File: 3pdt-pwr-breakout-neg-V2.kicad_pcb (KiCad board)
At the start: 2 copper layers, 40 x 21.5 mm, 42 parts, among them Q1 DMP3099L, SW1 SW_3PDT, U1 TLV76701DRVR, U2 LM2664M6X/NOPB, U3 LM2664M6X/NOPB

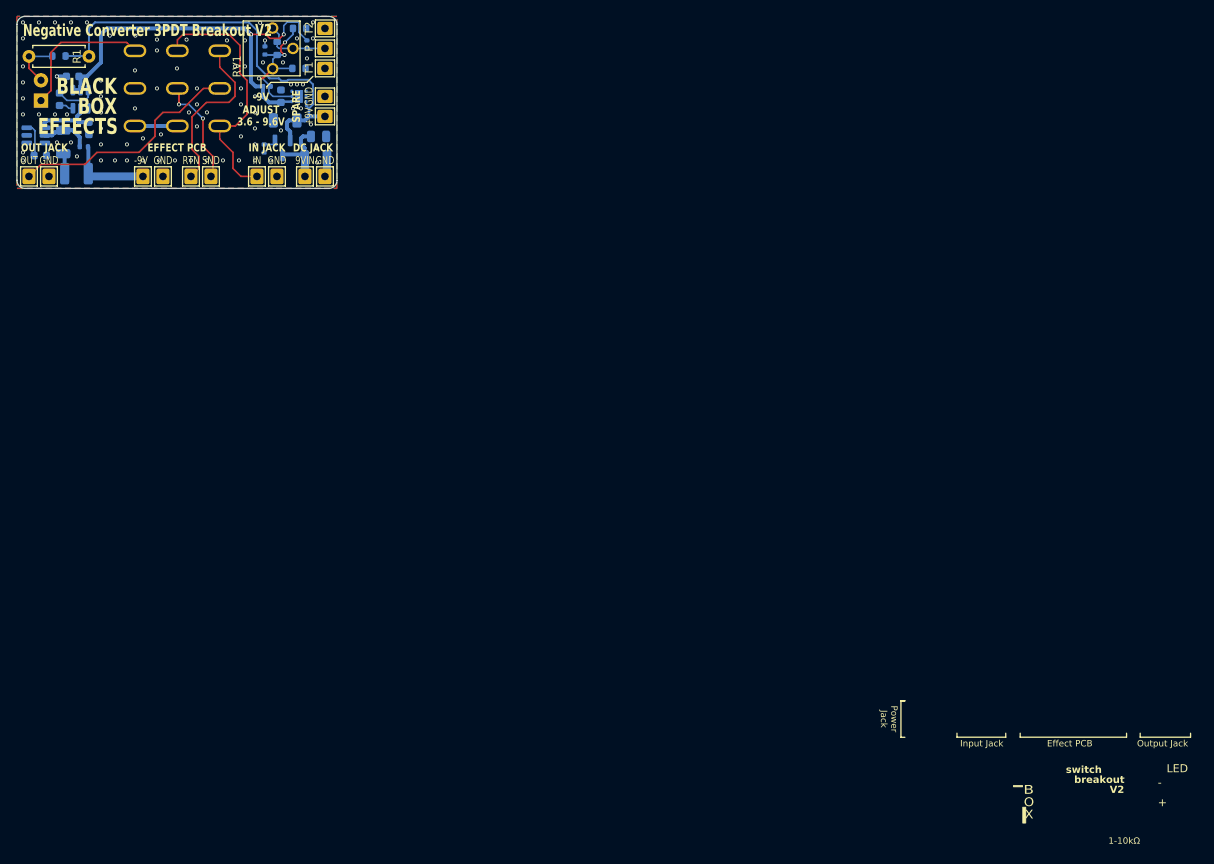
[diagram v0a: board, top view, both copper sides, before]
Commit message: Moved wire pads, clearing warnings. Good to fab?
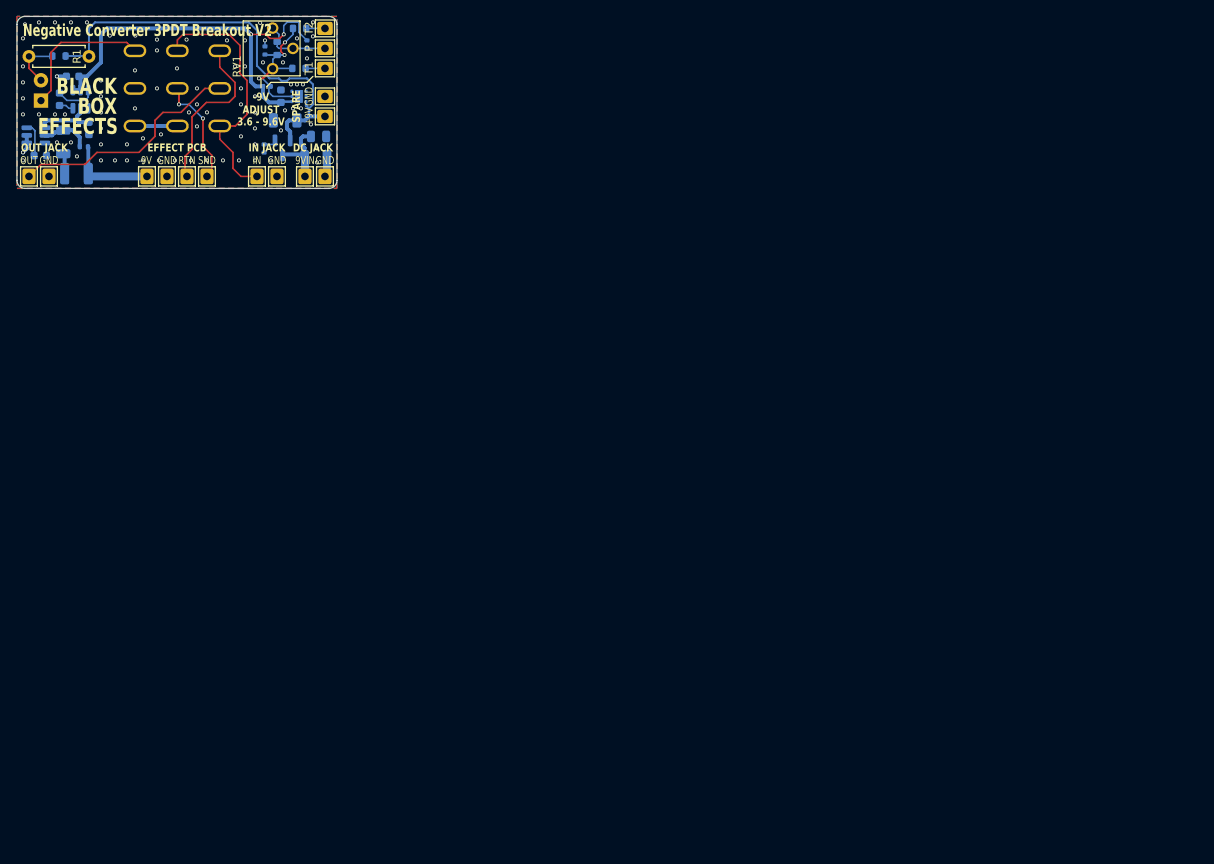
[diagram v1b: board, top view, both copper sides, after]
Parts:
- C10, C4, C5, C7: value 2.2u -> 1u
- moved WP10 0.50 mm to (66.2, 71.0)
- moved WP7 0.50 mm to (68.8, 71.0)
- moved WP8 0.50 mm to (71.2, 71.0)
- moved WP9 0.50 mm to (63.8, 71.0)
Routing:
- net Net-(R7-Pad1): track 0.00 -> 2.42 mm
- net Net-(R8-Pad1): track 0.00 -> 2.35 mm
- net GND: track 7.37 -> 9.69 mm
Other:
- board text removed: "+"
- board text removed: "-"
- board text removed: "1-10kΩ"
- board text removed: "B"
- board text removed: "Effect PCB"
- board text removed: "Input Jack"
- board text removed: "O"
- board text removed: "Output Jack"
- board text removed: "Power Jack"
- board text removed: "V2"
- board text removed: "X"
- board text removed: "breakout"
- board text removed: "switch"

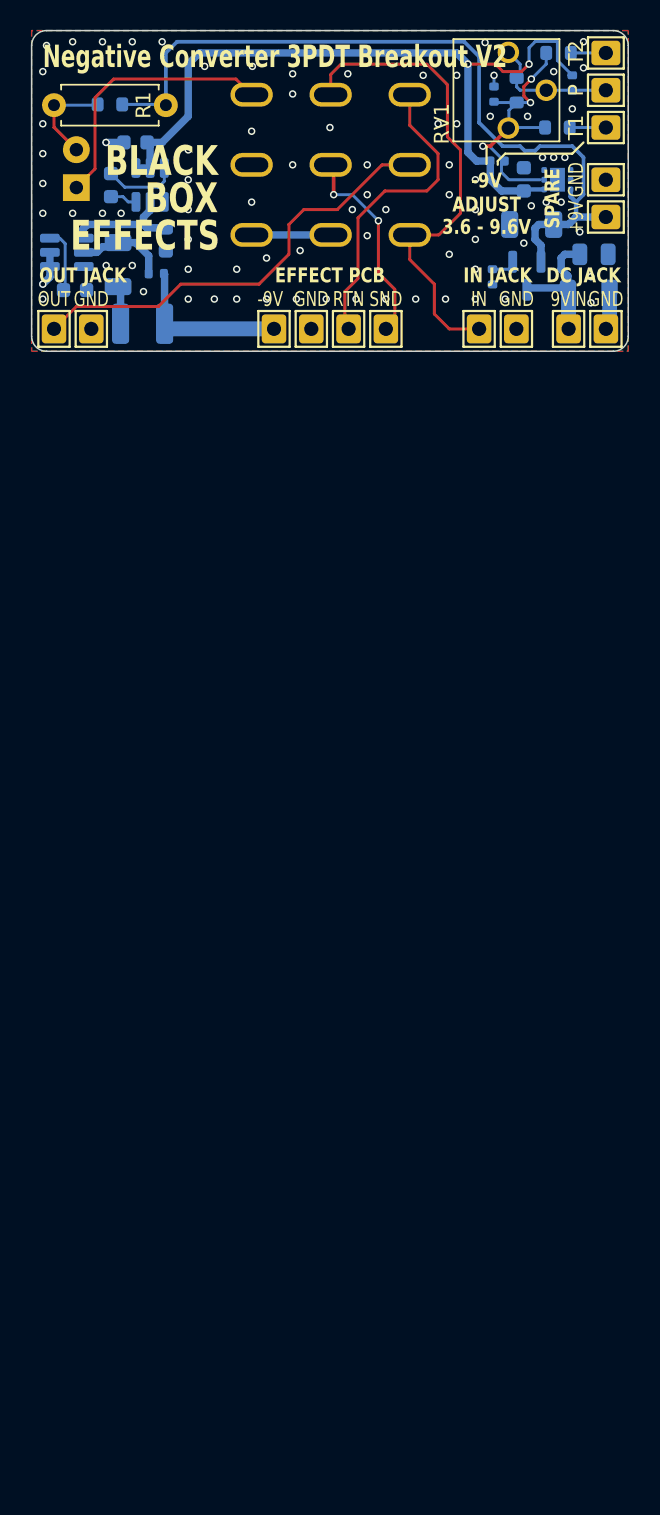
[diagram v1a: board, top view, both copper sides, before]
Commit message: Changed LDO and added negative LDO
Changed LDO to a leaded package and added an optional negative LDO. Layout changes implemented, going to review and order.
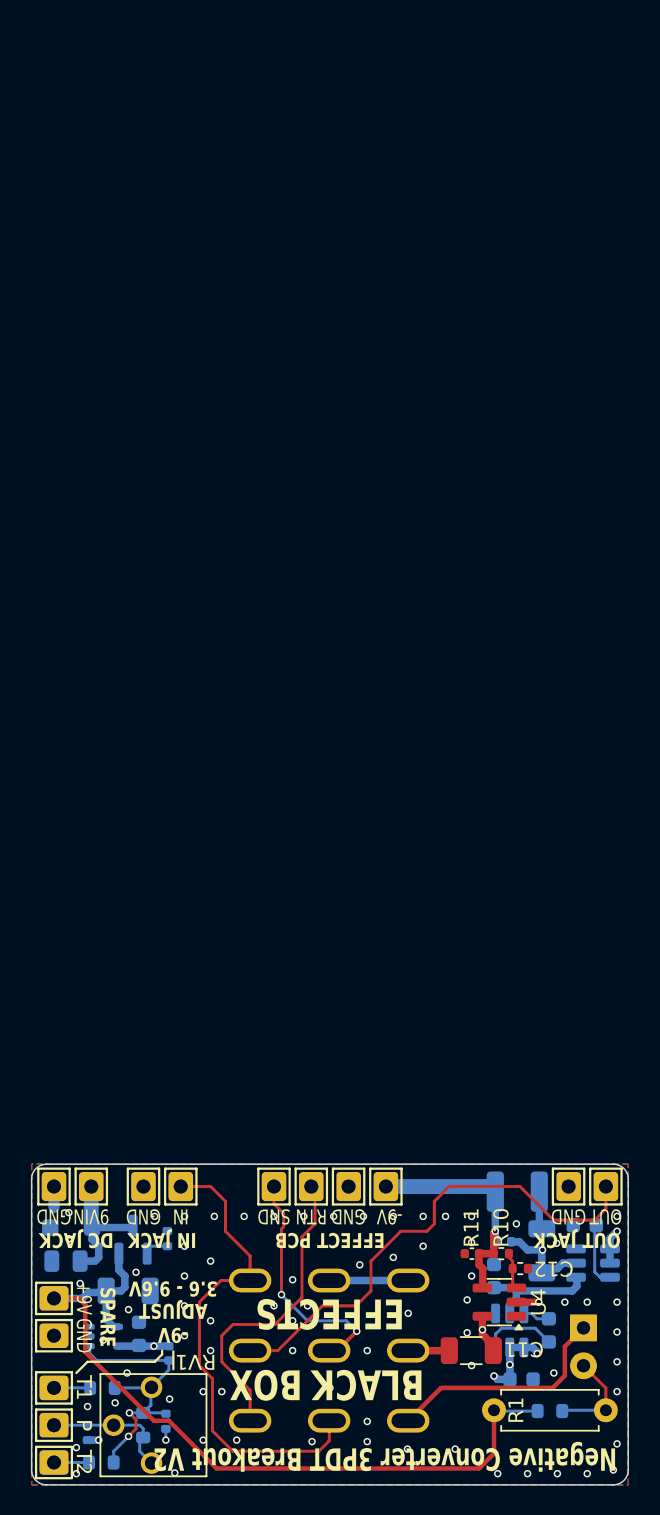
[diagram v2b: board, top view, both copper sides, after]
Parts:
- added C11: 2.2u, Capacitor_SMD:C_1206_3216Metric, F.Cu at (77.0, 139.5)
- added C12: 100n, Capacitor_SMD:C_0402_1005Metric, F.Cu at (77.0, 133.0)
- added R10: 30k, Resistor_SMD:R_0402_1005Metric, F.Cu at (80.3, 134.0)
- added R11: 4.7k, Resistor_SMD:R_0402_1005Metric, F.Cu at (79.0, 133.0)
- added U4: MIC5270YM5-TR, Package_TO_SOT_SMD:SOT-23-5, F.Cu at (78.9, 136.2)
- R4: value 36k -> 22k
- R8: value 82k -> 47k
- U1: value TLV76701DRVR -> TPS71501DCKRM3; footprint Package_SON:WSON-6-1EP_2x2mm_P0.65mm_EP1x1.6mm -> Package_TO_SOT_SMD:SOT-353_SC-70-5
- moved WP15 101.5 mm to (49.0, 147.0), turned to -90 degrees
- moved R8 99.3 mm to (52.2, 147.0), turned to 0 degrees
- moved WP13 96.8 mm to (49.0, 144.5), turned to -90 degrees
- moved R4 96.1 mm to (51.2, 145.0), turned to 90 degrees
- moved R6 92.9 mm to (55.0, 144.5), turned to 90 degrees
- moved RV1 92.6 mm to (55.5, 144.5), turned to -90 degrees
- moved R2 92.4 mm to (82.2, 143.6), turned to 0 degrees
- moved WP14 92.2 mm to (49.0, 142.0), turned to -90 degrees
- moved R5 91.7 mm to (56.5, 144.2), turned to -90 degrees
- moved R1 90.2 mm to (78.5, 143.5), turned to 0 degrees
- moved R7 89.8 mm to (52.2, 142.0), turned to 0 degrees
- moved C4 86.9 mm to (80.3, 141.4), turned to 180 degrees
- moved WP12 85.9 mm to (49.0, 138.5), turned to 90 degrees
- moved D2 83.7 mm to (84.5, 138.0), turned to -90 degrees
- moved U1 83.3 mm to (52.4, 138.6)
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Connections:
- U1 pad 1: +4V5 -> /FB
- U1 pad 2: /FB -> GND
- U1 pad 3: GND -> unconnected-(U1-NC-Pad3)
- U1 pad 4: unconnected-(U1-EN-Pad4) -> +9V
- U1 pad 5: GND -> +4V5
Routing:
- net +4V5: track 52.6 -> 9.78 mm, vias 2 -> 5
- net -9V_PRE: track 6.24 -> 16.7 mm, vias 0 -> 2
- net GND: track 9.69 -> 16.0 mm, vias 82 -> 77
- net -9V: track 10.4 -> 15.3 mm, vias 0 -> 1
- net /OUT: track 29.6 -> 33.2 mm
- net /LED-: track 18.0 -> 15.5 mm
- net /SEND: track 13.8 -> 16.0 mm
- net Net-(U4-ADJ): track 0.00 -> 2.26 mm
- net +9V: track 53.5 -> 52.7 mm
- net /FB: track 18.3 -> 19.0 mm, vias 3 -> 2
- added copper zone on In1.Cu, net +4V5
- added copper zone on In1.Cu, net GND
- added copper zone on In2.Cu, net GND
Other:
- copper layers 2 -> 4
